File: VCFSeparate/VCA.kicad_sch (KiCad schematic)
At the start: 1 part, among them U3 LM13700

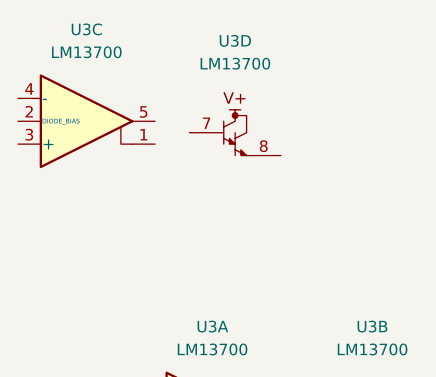
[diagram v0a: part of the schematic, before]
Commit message: VCFSeparate
レゾナンスVCAを追加
コントローラー系を作成中
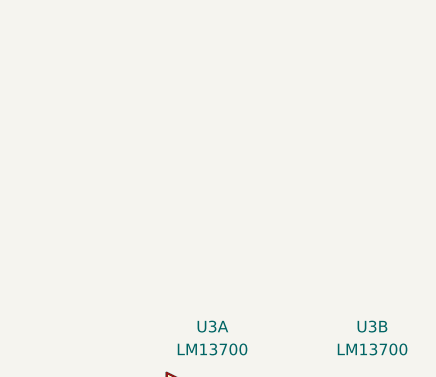
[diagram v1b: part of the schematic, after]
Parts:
- removed unit 4 of U3
- removed unit 3 of U3
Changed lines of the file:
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@@
-	(symbol
-		(lib_id "Amplifier_Operational:LM13700")
-		(at 72.39 41.91 0)
-		(unit 4)
-		(exclude_from_sim no)
-		(in_bom yes)
-		(on_board yes)
-		(dnp no)
-		(fields_autoplaced yes)
-		(property "Reference" "U3"
-			(at 69.85 31.75 0)
-			(effects
-				(font
-					(size 1.27 1.27)
-				)
-			)
-		)
-		(property "Value" "LM13700"
-			(at 69.85 34.29 0)
-			(effects
-				(font
-					(size 1.27 1.27)
-				)
-			)
-		)
-		(property "Footprint" "Package_SO:SOIC-16_3.9x9.9mm_P1.27mm"
-			(at 64.77 41.275 0)
-			(effects
-				(font
-					(size 1.27 1.27)
-				)
-				(hide yes)
-			)
-		)
-		(property "Datasheet" "http://www.ti.com/lit/ds/symlink/lm13700.pdf"
-			(at 64.77 41.275 0)
-			(effects
-				(font
-					(size 1.27 1.27)
-				)
-				(hide yes)
-			)
-		)
-		(property "Description" "Dual Operational Transconductance Amplifiers with Linearizing Diodes and Buffers, DIP-16/SOIC-16"
-			(at 72.39 41.91 0)
-			(effects
-				(font
-					(size 1.27 1.27)
-				)
-				(hide yes)
-			)
-		)
-		(pin "15"
-		)
-		(pin "2"
-		)
-		(pin "7"
-		)
-		(pin "11"
-		)
-		(pin "10"
-		)
-		(pin "4"
-		)
-		(pin "13"
-		)
-		(pin "1"
-		)
-		(pin "12"
-		)
-		(pin "14"
-		)
-		(pin "5"
-		)
-		(pin "16"
-		)
-		(pin "8"
-		)
-		(pin "9"
-		)
-		(pin "3"
-		)
-		(pin "6"
-		)
-		(instances
-			(project "VCFSeparate"
-				(path "/02fc5d1f-a2a3-4ec9-a454-0bdd0b1ddad0/7a121d15-c28a-4311-ac58-5e9e0128534b"
-					(reference "U3")
-					(unit 4)
-				)
-			)
-		)
-	)
 	(symbol
 		(lib_id "Amplifier_Operational:LM13700")
@@
 				)
 			)
-		)
-	)
-	(symbol
-		(lib_id "Amplifier_Operational:LM13700")
-		(at 53.34 40.64 0)
-		(unit 3)
-		(exclude_from_sim no)
-		(in_bom yes)
-		(on_board yes)
-		(dnp no)
-		(fields_autoplaced yes)
-		(property "Reference" "U3"
-			(at 53.34 30.48 0)
-			(effects
-				(font
-					(size 1.27 1.27)
-				)
-			)
-		)
-		(property "Value" "LM13700"
-			(at 53.34 33.02 0)
-			(effects
-				(font
-					(size 1.27 1.27)
-				)
-			)
-		)
-		(property "Footprint" "Package_SO:SOIC-16_3.9x9.9mm_P1.27mm"
-			(at 45.72 40.005 0)
-			(effects
-				(font
-					(size 1.27 1.27)
-				)
-				(hide yes)
-			)
-		)
-		(property "Datasheet" "http://www.ti.com/lit/ds/symlink/lm13700.pdf"
-			(at 45.72 40.005 0)
-			(effects
-				(font
-					(size 1.27 1.27)
-				)
-				(hide yes)
-			)
-		)
-		(property "Description" "Dual Operational Transconductance Amplifiers with Linearizing Diodes and Buffers, DIP-16/SOIC-16"
-			(at 53.34 40.64 0)
-			(effects
-				(font
-					(size 1.27 1.27)
-				)
-				(hide yes)
-			)
-		)
-		(pin "15"
-		)
-		(pin "2"
-		)
-		(pin "7"
-		)
-		(pin "11"
-		)
-		(pin "10"
-		)
-		(pin "4"
-		)
-		(pin "13"
-		)
-		(pin "1"
-		)
-		(pin "12"
-		)
-		(pin "14"
-		)
-		(pin "5"
-		)
-		(pin "16"
-		)
-		(pin "8"
-		)
-		(pin "9"
-		)
-		(pin "3"
-		)
-		(pin "6"
-		)
-		(instances
-			(project "VCFSeparate"
-				(path "/02fc5d1f-a2a3-4ec9-a454-0bdd0b1ddad0/7a121d15-c28a-4311-ac58-5e9e0128534b"
-					(reference "U3")
-					(unit 3)
-				)
-			)

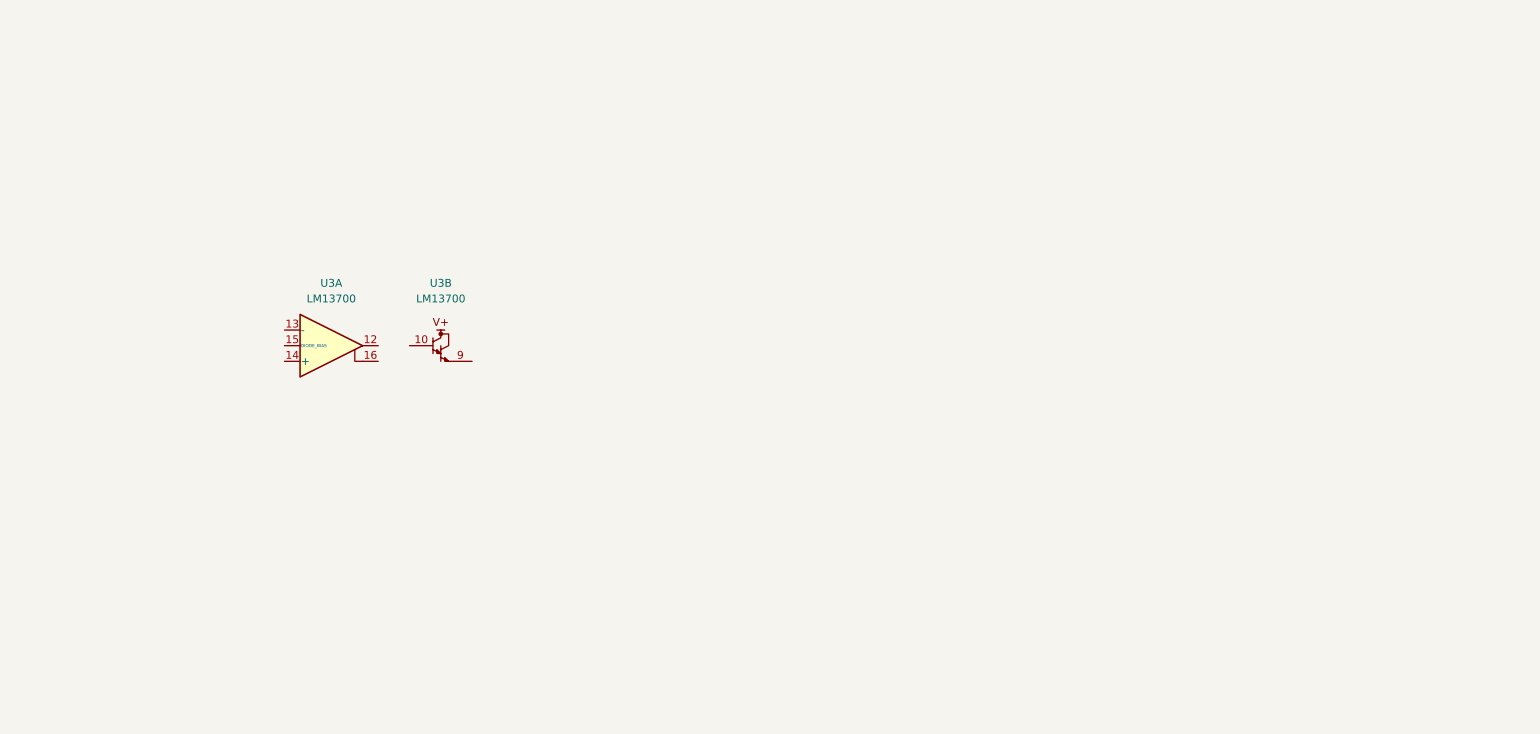
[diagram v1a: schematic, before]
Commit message: MC2
VCO,VCF+VCA,Powerを登録
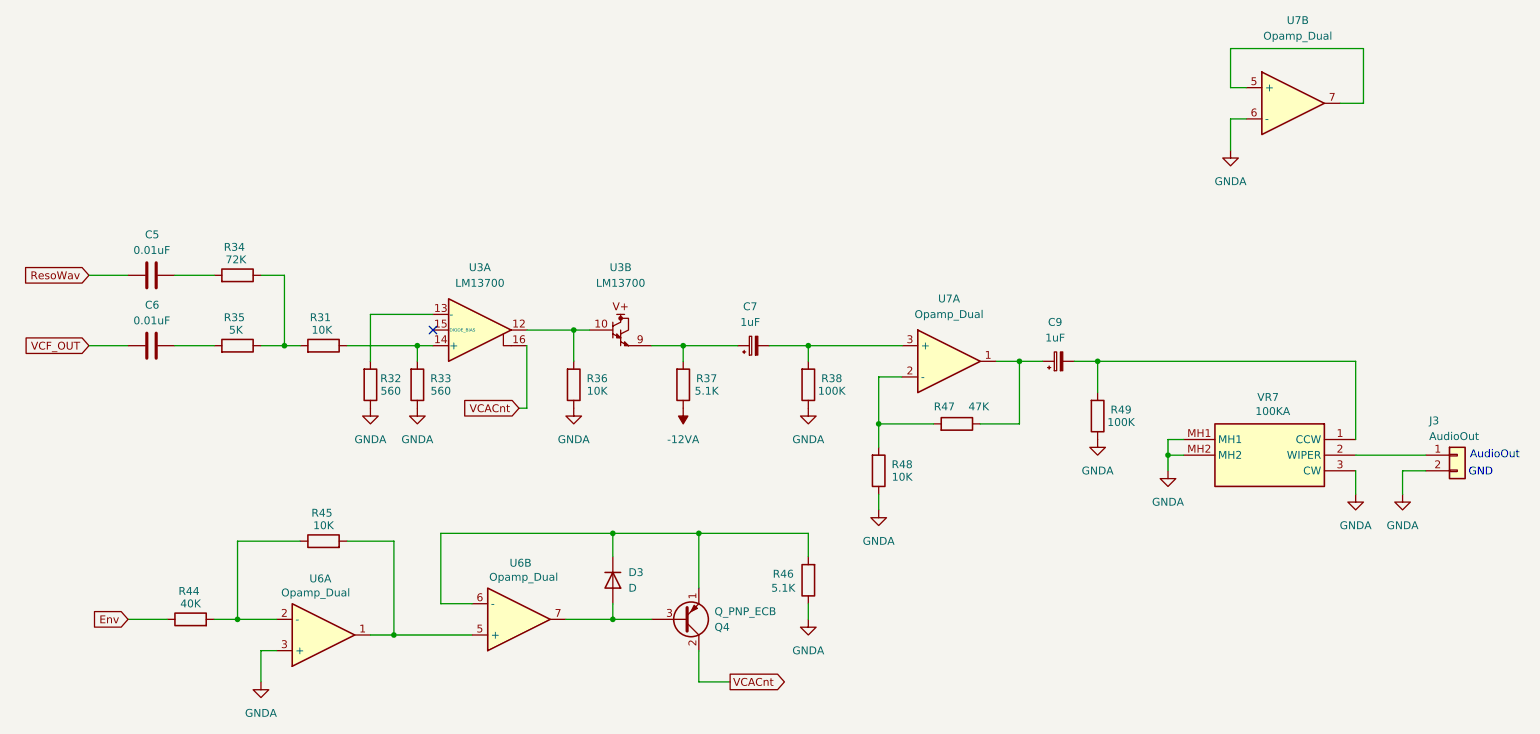
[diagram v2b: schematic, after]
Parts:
- added C5, C6: 0.01uF, Capacitor_THT:C_Disc_D3.4mm_W2.1mm_P2.50mm, symbol Device:C
- added C7, C9: 1uF, Capacitor_THT:CP_Radial_D5.0mm_P2.50mm, symbol Device:C_Polarized_Small
- added D3: D, Diode_THT:D_DO-35_SOD27_P2.54mm_Vertical_AnodeUp, symbol Device:D
- added J3: AudioOut, Connector_PinHeader_2.54mm:PinHeader_1x02_P2.54mm_Vertical, symbol Connector_Generic:Conn_01x02
- added Q4: Q_PNP_ECB, Package_TO_SOT_THT:TO-92_HandSolder, symbol Device:Q_PNP_ECB
- added R31, R36, R45, R48: 10K, Resistor_THT:R_Axial_DIN0204_L3.6mm_D1.6mm_P2.54mm_Vertical, symbol Device:R
- added R32, R33: 560, Resistor_THT:R_Axial_DIN0204_L3.6mm_D1.6mm_P2.54mm_Vertical, symbol Device:R
- added R34: 72K, Resistor_THT:R_Axial_DIN0204_L3.6mm_D1.6mm_P2.54mm_Vertical, symbol Device:R
- added R35: 5K, Resistor_THT:R_Axial_DIN0204_L3.6mm_D1.6mm_P2.54mm_Vertical, symbol Device:R
- added R37, R46: 5.1K, Resistor_THT:R_Axial_DIN0204_L3.6mm_D1.6mm_P2.54mm_Vertical, symbol Device:R
- added R38, R49: 100K, Resistor_THT:R_Axial_DIN0204_L3.6mm_D1.6mm_P2.54mm_Vertical, symbol Device:R
- added R44: 40K, Resistor_THT:R_Axial_DIN0204_L3.6mm_D1.6mm_P2.54mm_Vertical, symbol Device:R
- added R47: 47K, Resistor_THT:R_Axial_DIN0204_L3.6mm_D1.6mm_P2.54mm_Vertical, symbol Device:R
- added U6, U7: Opamp_Dual, Package_SO:SO-8_3.9x4.9mm_P1.27mm, symbol Device:Opamp_Dual
- added VR7: 100KA, RK09D117000B, symbol SamacSys_Parts:RK09D117000B
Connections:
- net at U3.12: now also U3.10, R36.2
- net at U3.13 (-): now also R32.2
- net at U3.14 (+): now also R31.1, R33.2
- net VCACnt: now reaches U3.16
- net VCACnt: now also Q4.2 (C)
- net at U3.9: now also C7.1, R37.2
- new net: R44.2, R45.1, U6.2 (-)
- new net: R45.2, U6.1, U6.5 (+)
- new net: C9.1, R47.1, U7.1
- new net: R47.2, R48.2, U7.2 (-)
- new net: D3.1 (K), Q4.1 (E), R46.2, U6.6 (-)
- new net: D3.2 (A), Q4.3 (B), U6.7
- new net: C7.2, R38.2, U7.3 (+)
- new net: R31.2, R34.1, R35.1
- new net: C9.2, R49.2, VR7.1 (CCW)
- new net: J3.1 (Pin_1), VR7.2 (WIPER)
- new net: U7.5 (+), U7.7
- new net: C5.2, R34.2
- new net: C6.2, R35.2
- new net -12VA: R37.1
- new net Env: R44.1
- new net GNDA: J3.2 (Pin_2), R32.1, R33.1, R36.1, R38.1, R46.1, R48.1, R49.1, U6.3 (+), U7.6 (-), VR7.3 (CW), VR7.MH1, VR7.MH2
- new net ResoWav: C5.1
- new net VCF_OUT: C6.1
- no-connect marks 0 -> 1
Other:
- note added: "AudioOut"
- note added: "GND"
- moved on the sheet: U3A, U3B

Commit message: MC2
ここまででFIXした内容
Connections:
- net Env renamed VCAEnv
